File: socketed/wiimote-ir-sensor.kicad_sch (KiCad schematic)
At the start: 10 parts, among them J1 Conn_01x04_Pin, U2 AP2112-3.3V, X1 SG3225CAN 24.0000M-TJGA3

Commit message: Socketed board: Tidy up
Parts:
- R13: value 330K -> 33K

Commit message: More QoL tweaks to socketed board
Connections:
- net +5V: now also J1.4 (Pin_4); no longer J1.1 (Pin_1)
- net GND: now also J1.1 (Pin_1); no longer J1.4 (Pin_4)
- net SCL: now also R8.2; no longer R9.1
- net SDA: now also R9.1; no longer R8.2
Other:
- moved on the sheet: R8, R9
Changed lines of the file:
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@@
 	(symbol
 		(lib_id "power:+5V")
-		(at 76.2 76.2 270)
+		(at 76.2 88.9 270)
 		(unit 1)
 		(exclude_from_sim no)
@@
 		(fields_autoplaced yes)
 		(property "Reference" "#PWR03"
-			(at 72.39 76.2 0)
+			(at 72.39 88.9 0)
 			(effects
 				(font
@@
 		)
 		(property "Value" "+5V"
-			(at 80.01 76.835 90)
+			(at 80.01 88.8999 90)
 			(effects
 				(font
@@
 		)
 		(property "Footprint" ""
-			(at 76.2 76.2 0)
+			(at 76.2 88.9 0)
 			(effects
 				(font
@@
 		)
 		(property "Datasheet" ""
-			(at 76.2 76.2 0)
-			(effects
-				(font
-					(size 1.27 1.27)
-				)
-				(hide yes)
-			)
-		)
-		(property "Description" ""
-			(at 76.2 76.2 0)
+			(at 76.2 88.9 0)
+			(effects
+				(font
+					(size 1.27 1.27)
+				)
+				(hide yes)
+			)
+		)
+		(property "Description" ""
+			(at 76.2 88.9 0)
 			(effects
 				(font
@@
 	(symbol
 		(lib_id "Device:R")
-		(at 118.11 81.28 0)
+		(at 132.08 81.28 0)
 		(unit 1)
 		(exclude_from_sim no)
@@
 		(fields_autoplaced yes)
 		(property "Reference" "R8"
-			(at 120.65 80.645 0)
+			(at 134.62 80.0099 0)
 			(effects
 				(font
@@
 		)
 		(property "Value" "2.7K"
-			(at 120.65 83.185 0)
+			(at 134.62 82.5499 0)
 			(effects
 				(font
@@
 		)
 		(property "Footprint" "Resistor_SMD:R_0603_1608Metric_Pad0.98x0.95mm_HandSolder"
-			(at 116.332 81.28 90)
+			(at 130.302 81.28 90)
 			(effects
 				(font
@@
 		)
 		(property "Datasheet" "~"
-			(at 118.11 81.28 0)
-			(effects
-				(font
-					(size 1.27 1.27)
-				)
-				(hide yes)
-			)
-		)
-		(property "Description" ""
-			(at 118.11 81.28 0)
+			(at 132.08 81.28 0)
+			(effects
+				(font
+					(size 1.27 1.27)
+				)
+				(hide yes)
+			)
+		)
+		(property "Description" ""
+			(at 132.08 81.28 0)
 			(effects
 				(font
@@
 	(symbol
 		(lib_id "Device:R")
-		(at 132.08 81.28 180)
+		(at 118.11 81.28 180)
 		(unit 1)
 		(exclude_from_sim no)
@@
 		(fields_autoplaced yes)
 		(property "Reference" "R9"
-			(at 134.62 80.645 0)
+			(at 120.65 80.0099 0)
 			(effects
 				(font
@@
 		)
 		(property "Value" "2.7K"
-			(at 134.62 83.185 0)
+			(at 120.65 82.5499 0)
 			(effects
 				(font
@@
 		)
 		(property "Footprint" "Resistor_SMD:R_0603_1608Metric_Pad0.98x0.95mm_HandSolder"
-			(at 133.858 81.28 90)
+			(at 119.888 81.28 90)
 			(effects
 				(font
@@
 		)
 		(property "Datasheet" "~"
-			(at 132.08 81.28 0)
-			(effects
-				(font
-					(size 1.27 1.27)
-				)
-				(hide yes)
-			)
-		)
-		(property "Description" ""
-			(at 132.08 81.28 0)
+			(at 118.11 81.28 0)
+			(effects
+				(font
+					(size 1.27 1.27)
+				)
+				(hide yes)
+			)
+		)
+		(property "Description" ""
+			(at 118.11 81.28 0)
 			(effects
 				(font
@@
 	(symbol
 		(lib_id "power:GND")
-		(at 76.2 88.9 90)
+		(at 76.2 76.2 90)
 		(unit 1)
 		(exclude_from_sim no)
@@
 		(dnp no)
 		(property "Reference" "#GND014"
-			(at 76.2 88.9 0)
+			(at 76.2 76.2 0)
 			(effects
 				(font
@@
 		)
 		(property "Value" "GND"
-			(at 78.74 88.9 0)
+			(at 78.74 76.2 0)
 			(effects
 				(font
@@
 		)
 		(property "Footprint" ""
-			(at 76.2 88.9 0)
+			(at 76.2 76.2 0)
 			(effects
 				(font
@@
 		)
 		(property "Datasheet" ""
-			(at 76.2 88.9 0)
-			(effects
-				(font
-					(size 1.27 1.27)
-				)
-				(hide yes)
-			)
-		)
-		(property "Description" ""
-			(at 76.2 88.9 0)
-			(effects
-				(font
+			(at 76.2 76.2 0)
+			(effects
+				(font
+					(size 1.27 1.27)
+				)
+				(hide yes)
+			)
+		)
+		(property "Description" ""
+			(at 76.2 76.2 0)
+			(effects
+				(font

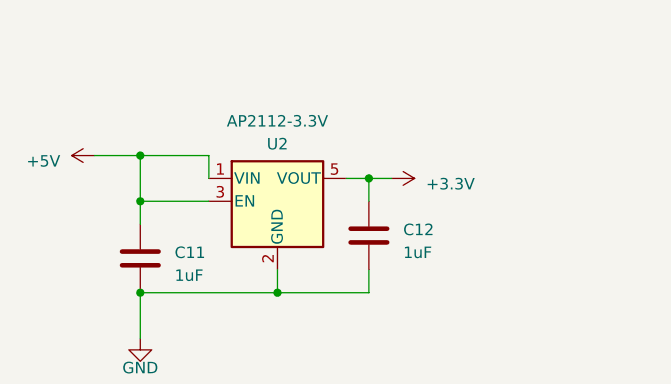
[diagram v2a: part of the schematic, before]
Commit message: Update socketed board - cleanup and add jumper to skip regulator
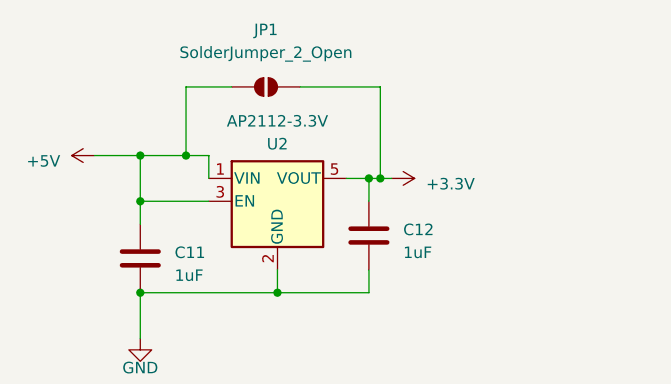
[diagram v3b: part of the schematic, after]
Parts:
- added JP1: SolderJumper_2_Open, Jumper:SolderJumper-2_P1.3mm_Open_RoundedPad1.0x1.5mm, symbol Jumper:SolderJumper_2_Open
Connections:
- net +3.3V: now also JP1.2 (B)
- net +5V: now also JP1.1 (A)
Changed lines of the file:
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@@
+	)
+	(junction
+		(at 69.85 41.91)
+		(diameter 0)
+		(color 0 0 0 0)
+	)
+	(junction
+		(at 91.44 44.45)
+		(diameter 0)
+		(color 0 0 0 0)
 	)
 	(junction
@@
 	(wire
 		(pts
+			(xy 91.44 44.45) (xy 92.71 44.45)
+		)
+		(stroke
+			(width 0)
+			(type default)
+		)
+	)
+	(wire
+		(pts
 			(xy 114.3 101.6) (xy 147.32 101.6)
 		)
@@
 	(wire
 		(pts
+			(xy 69.85 34.29) (xy 74.93 34.29)
+		)
+		(stroke
+			(width 0)
+			(type default)
+		)
+	)
+	(wire
+		(pts
 			(xy 69.85 81.28) (xy 72.39 81.28)
 		)
@@
 	(wire
 		(pts
+			(xy 69.85 41.91) (xy 72.39 41.91)
+		)
+		(stroke
+			(width 0)
+			(type default)
+		)
+	)
+	(wire
+		(pts
 			(xy 132.08 76.2) (xy 132.08 77.47)
 		)
@@
 	(wire
 		(pts
+			(xy 91.44 34.29) (xy 91.44 44.45)
+		)
+		(stroke
+			(width 0)
+			(type default)
+		)
+	)
+	(wire
+		(pts
 			(xy 80.01 57.15) (xy 64.77 57.15)
 		)
@@
 	(wire
 		(pts
-			(xy 64.77 41.91) (xy 72.39 41.91)
+			(xy 64.77 41.91) (xy 69.85 41.91)
 		)
 		(stroke
@@
 	(wire
 		(pts
+			(xy 69.85 41.91) (xy 69.85 34.29)
+		)
+		(stroke
+			(width 0)
+			(type default)
+		)
+	)
+	(wire
+		(pts
 			(xy 90.17 57.15) (xy 80.01 57.15)
 		)
@@
 	(wire
 		(pts
-			(xy 90.17 44.45) (xy 92.71 44.45)
+			(xy 90.17 44.45) (xy 91.44 44.45)
 		)
 		(stroke
@@
 		(pts
 			(xy 147.32 95.25) (xy 163.83 95.25)
+		)
+		(stroke
+			(width 0)
+			(type default)
+		)
+	)
+	(wire
+		(pts
+			(xy 82.55 34.29) (xy 91.44 34.29)
 		)
 		(stroke
@@
 					(unit 1)
 				)
+			)
+		)
+	)
+	(symbol
+		(lib_id "Jumper:SolderJumper_2_Open")
+		(at 78.74 34.29 0)
+		(unit 1)
+		(exclude_from_sim yes)
+		(in_bom no)
+		(on_board yes)
+		(dnp no)
+		(fields_autoplaced yes)
+		(property "Reference" "JP1"
+			(at 78.74 27.94 0)
+			(effects
+				(font
+					(size 1.27 1.27)
+				)
+			)
+		)
+		(property "Value" "SolderJumper_2_Open"
+			(at 78.74 30.48 0)
+			(effects
+				(font
+					(size 1.27 1.27)
+				)
+			)
+		)
+		(property "Footprint" "Jumper:SolderJumper-2_P1.3mm_Open_RoundedPad1.0x1.5mm"
+			(at 78.74 34.29 0)
+			(effects
+				(font
+					(size 1.27 1.27)
+				)
+				(hide yes)
+			)
+		)
+		(property "Datasheet" "~"
+			(at 78.74 34.29 0)
+			(effects
+				(font
+					(size 1.27 1.27)
+				)
+				(hide yes)
+			)
+		)
+		(property "Description" "Solder Jumper, 2-pole, open"
+			(at 78.74 34.29 0)
+			(effects
+				(font
+					(size 1.27 1.27)
+				)
+				(hide yes)
+			)
+		)
+		(pin "2"
+		)
+		(pin "1"
+		)
+		(instances
+			(project "wiimote-ir-sensor"
+				(path "/8863941e-bc94-45df-82a4-2b6eb6c570e3"
+					(reference "JP1")
+					(unit 1)
+				)
